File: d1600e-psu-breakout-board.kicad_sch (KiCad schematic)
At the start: 67 parts, among them J1 4PIN-22-27-2041, J10 10107844-002LF, J11 4PIN-22-27-2041, J12 4PIN-22-27-2041, J13 4PIN-22-27-2041, J14 4PIN-22-27-2041, J2 BM04B-SRSS-TB-LF-SN, J3 BM04B-SRSS-TB-LF-SN, J4 39288080, J5 39288080, J6 39288080, J7 39288080, J8 39288080, Q11 BC856,215

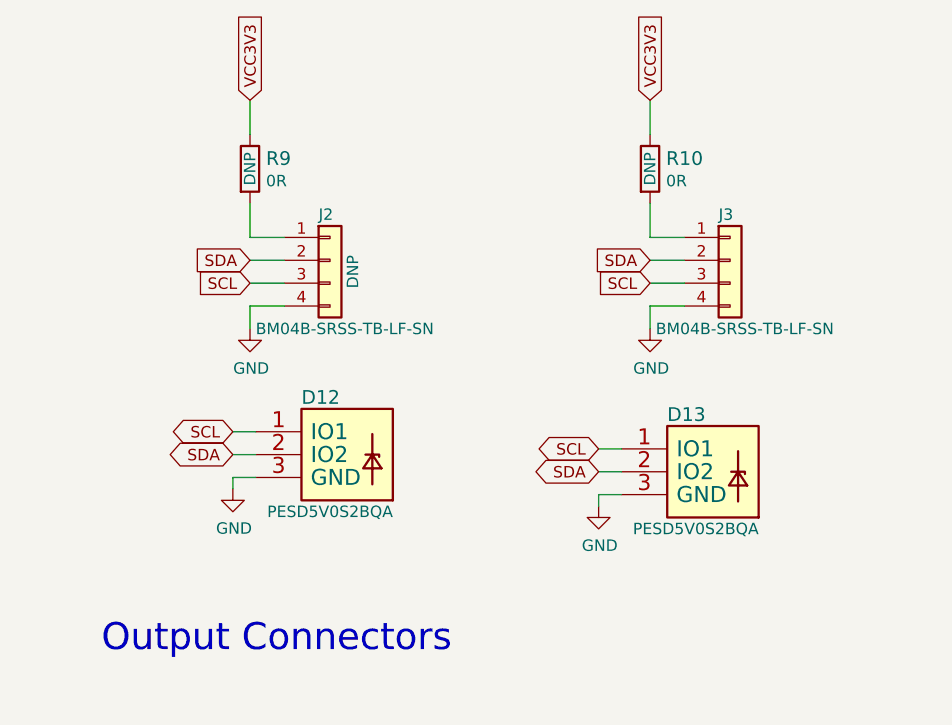
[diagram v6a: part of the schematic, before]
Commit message: #50436 Add FTDI led control, bump revision to 1.4.2
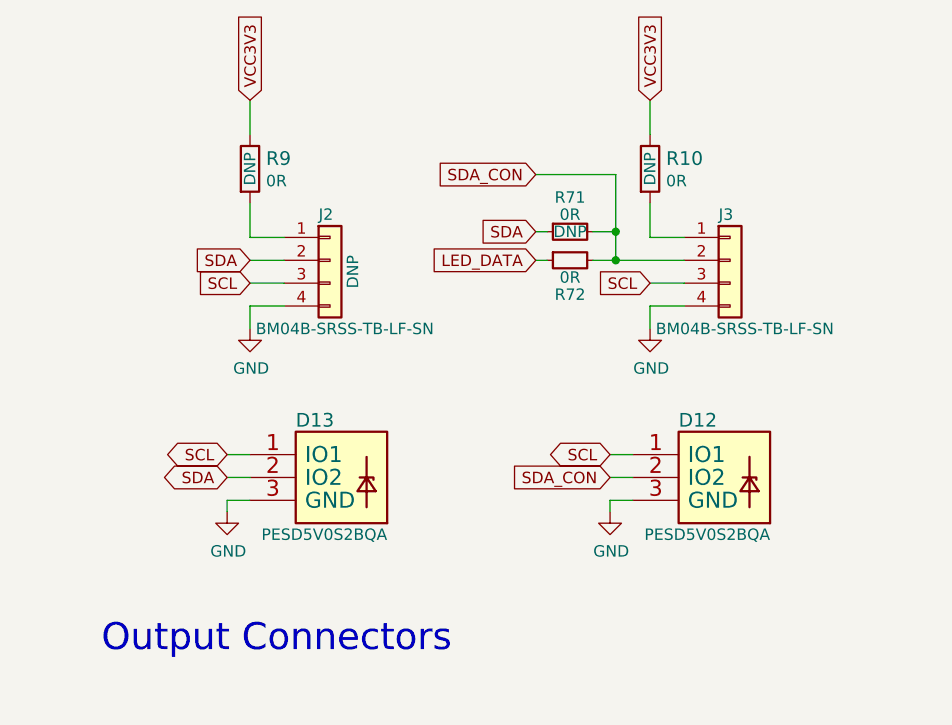
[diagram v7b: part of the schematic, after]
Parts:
- added R71, R72: R_0R_0402, antmicro-footprints:R_0402_1005Metric, symbol antmicroResistors0402:R_0R_0402
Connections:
- net SDA: now also R71.1; no longer D12.2 (IO2), J3.2 (Pin_2)
- new net LED_DATA: R72.1
- new net SDA_CON: D12.2 (IO2), J3.2 (Pin_2), R71.2, R72.2
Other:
- moved on the sheet: D12, D13

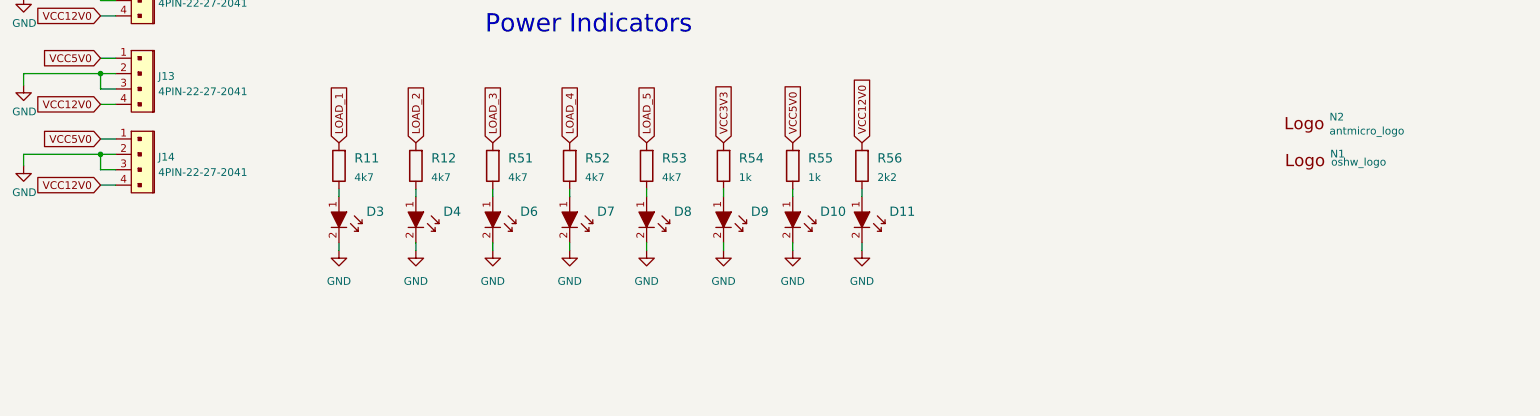
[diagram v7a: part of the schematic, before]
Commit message: #50436 Set U2 as DNP, add assembly variant table, bump to 1.4.3
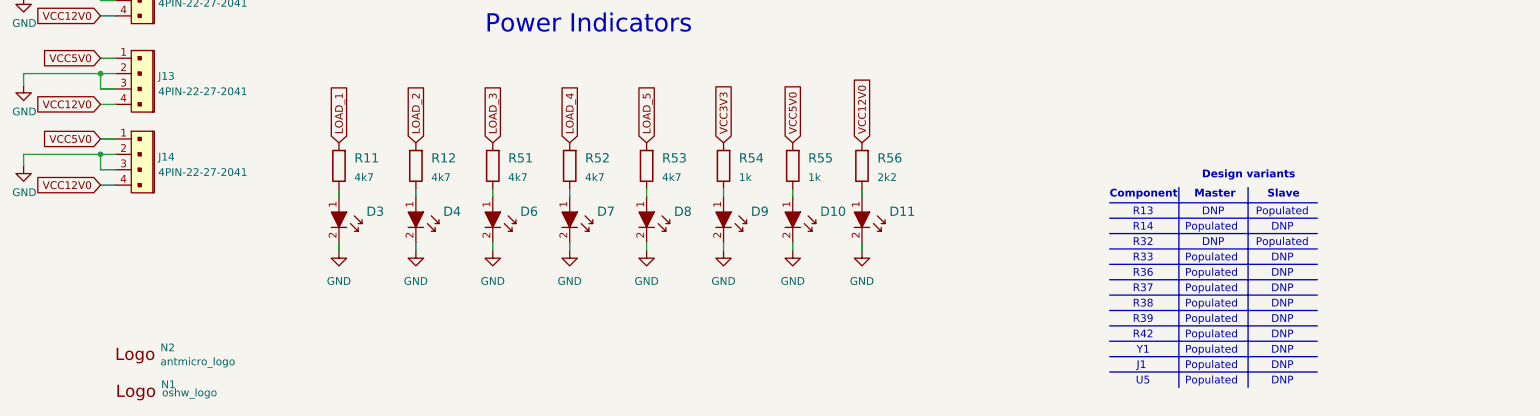
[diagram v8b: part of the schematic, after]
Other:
- note added: "Component"
- note added: "DNP"
- note added: "Design variants"
- note added: "J1"
- note added: "Master"
- note added: "Populated"
- note added: "R13"
- note added: "R14"
- note added: "R32"
- note added: "R33"
- note added: "R36"
- note added: "R37"
- note added: "R38"
- note added: "R39"
- note added: "R42"
- note added: "Slave"
- note added: "U5"
- note added: "Y1"
- moved on the sheet: N1, N2
